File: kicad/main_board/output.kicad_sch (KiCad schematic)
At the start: 12 parts, among them J10 CH4, J4 DRV1, J5 DRV2, J6 CH_IN, J7 CH1, J8 CH2, J9 CH3

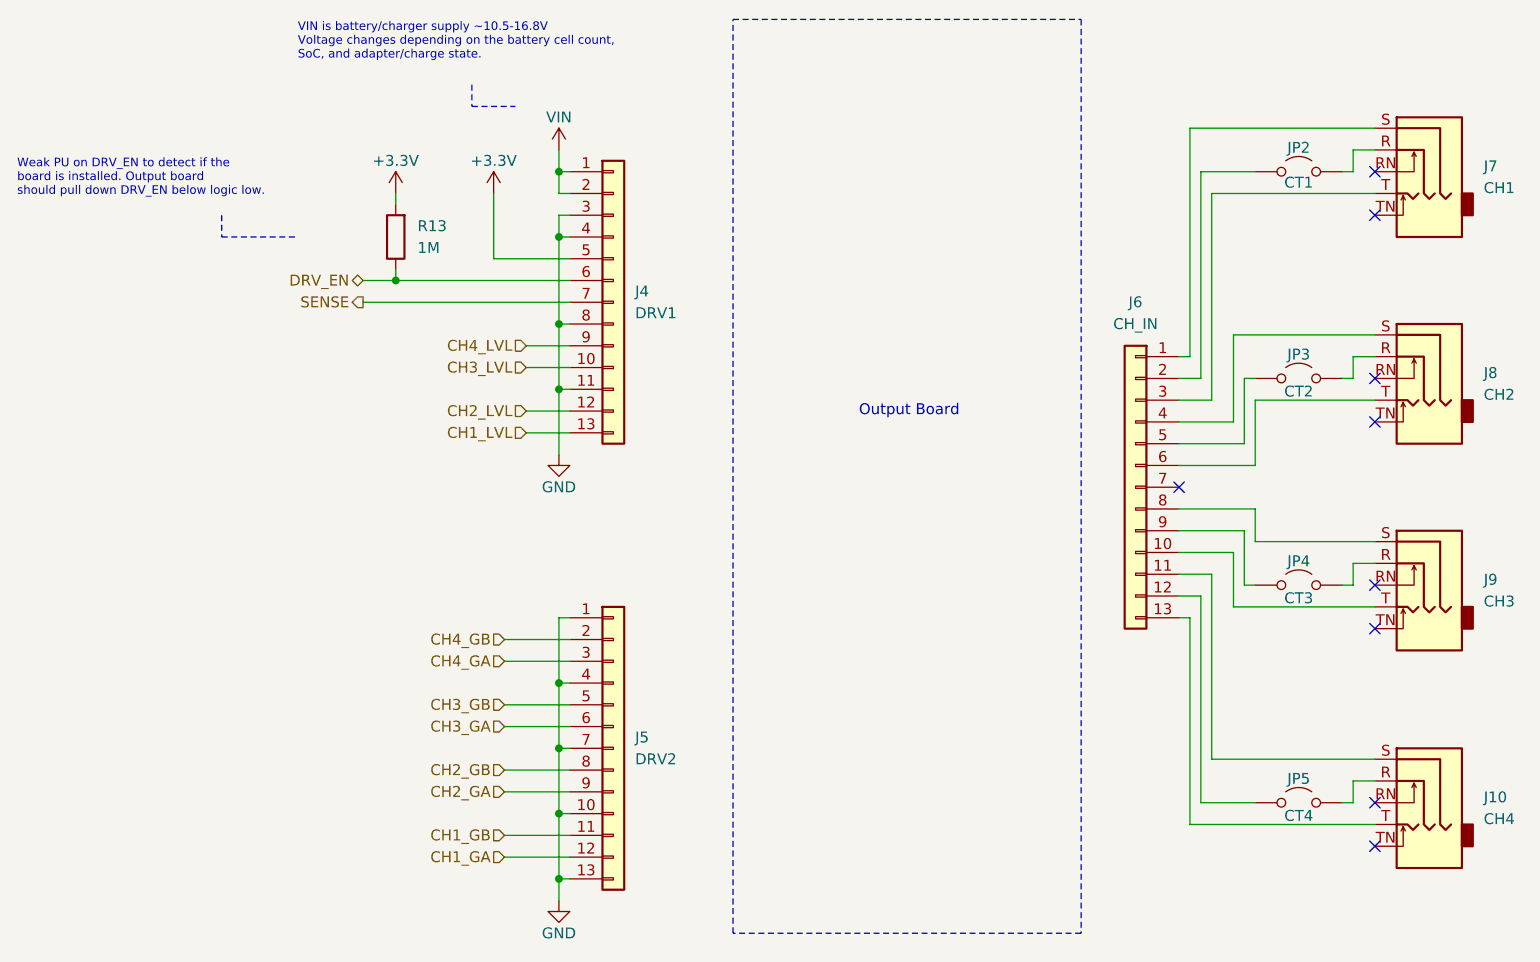
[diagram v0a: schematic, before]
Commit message: add input
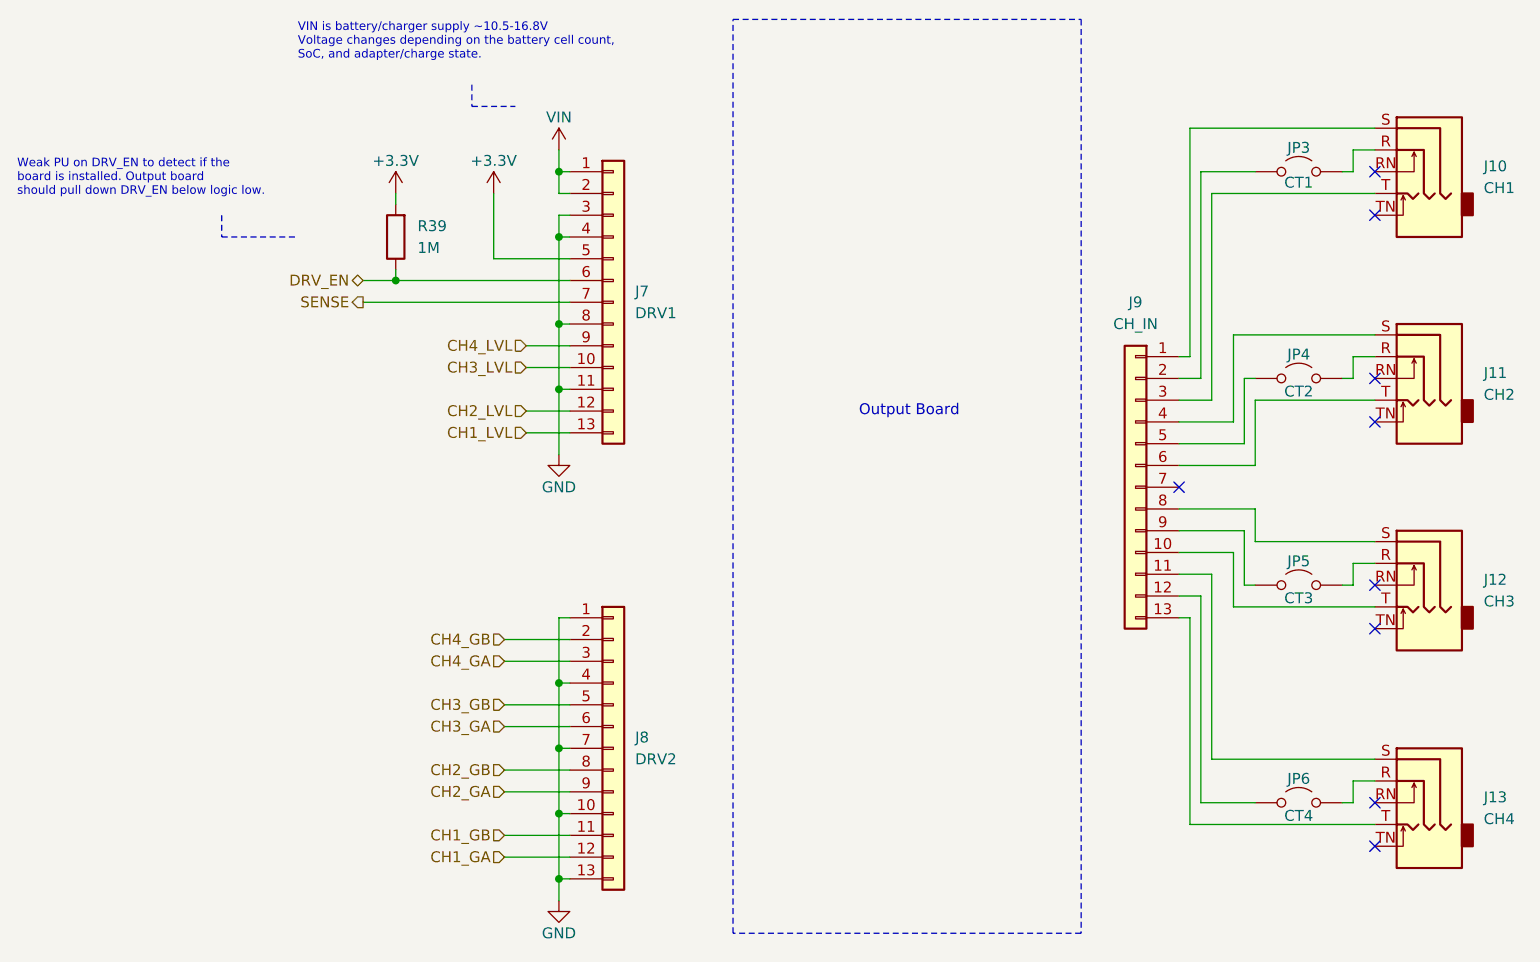
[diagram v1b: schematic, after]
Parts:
- renumbered J7 to J10, J8 to J11, J9 to J12, J10 to J13, J4 to J7, J5 to J8, J6 to J9, JP2 to JP3, JP3 to JP4, JP4 to JP5, JP5 to JP6, R13 to R39
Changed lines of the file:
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@@
 		(on_board yes)
 		(dnp no)
-		(property "Reference" "JP4"
+		(property "Reference" "JP5"
 			(at 198.12 101.346 0)
 			(effects
@@
 			(project "main_board"
 				(path "/8e1f1504-76c2-49e6-9261-3c1190503f8c/1327ee6b-7a00-44f7-81fe-b42319e4569a"
-					(reference "JP4")
+					(reference "JP5")
 					(unit 1)
 				)
@@
 		(dnp no)
 		(fields_autoplaced yes)
-		(property "Reference" "J4"
+		(property "Reference" "J7"
 			(at 120.65 69.8499 0)
 			(effects
@@
 			(project "main_board"
 				(path "/8e1f1504-76c2-49e6-9261-3c1190503f8c/1327ee6b-7a00-44f7-81fe-b42319e4569a"
-					(reference "J4")
+					(reference "J7")
 					(unit 1)
 				)
@@
 		(dnp no)
 		(fields_autoplaced yes)
-		(property "Reference" "J5"
+		(property "Reference" "J8"
 			(at 120.65 121.9199 0)
 			(effects
@@
 			(project "main_board"
 				(path "/8e1f1504-76c2-49e6-9261-3c1190503f8c/1327ee6b-7a00-44f7-81fe-b42319e4569a"
-					(reference "J5")
+					(reference "J8")
 					(unit 1)
 				)
@@
 		(on_board yes)
 		(dnp no)
-		(property "Reference" "#PWR041"
+		(property "Reference" "#PWR0105"
 			(at 111.76 147.32 0)
 			(effects
@@
 			(project "main_board"
 				(path "/8e1f1504-76c2-49e6-9261-3c1190503f8c/1327ee6b-7a00-44f7-81fe-b42319e4569a"
-					(reference "#PWR041")
+					(reference "#PWR0105")
 					(unit 1)
 				)
@@
 		(on_board yes)
 		(dnp no)
-		(property "Reference" "#PWR038"
+		(property "Reference" "#PWR0102"
 			(at 104.14 62.23 0)
 			(effects
@@
 			(project "main_board"
 				(path "/8e1f1504-76c2-49e6-9261-3c1190503f8c/1327ee6b-7a00-44f7-81fe-b42319e4569a"
-					(reference "#PWR038")
+					(reference "#PWR0102")
 					(unit 1)
 				)
@@
 		(on_board yes)
 		(dnp no)
-		(property "Reference" "JP5"
+		(property "Reference" "JP6"
 			(at 198.12 126.746 0)
 			(effects
@@
 			(project "main_board"
 				(path "/8e1f1504-76c2-49e6-9261-3c1190503f8c/1327ee6b-7a00-44f7-81fe-b42319e4569a"
-					(reference "JP5")
+					(reference "JP6")
 					(unit 1)
 				)
@@
 		(dnp no)
 		(fields_autoplaced yes)
-		(property "Reference" "J10"
+		(property "Reference" "J13"
 			(at 219.71 128.9049 0)
 			(effects
@@
 			(project "main_board"
 				(path "/8e1f1504-76c2-49e6-9261-3c1190503f8c/1327ee6b-7a00-44f7-81fe-b42319e4569a"
-					(reference "J10")
+					(reference "J13")
 					(unit 1)
 				)
@@
 		(dnp no)
 		(fields_autoplaced yes)
-		(property "Reference" "R13"
+		(property "Reference" "R39"
 			(at 95.25 62.2299 0)
 			(effects
@@
 			(project "main_board"
 				(path "/8e1f1504-76c2-49e6-9261-3c1190503f8c/1327ee6b-7a00-44f7-81fe-b42319e4569a"
-					(reference "R13")
+					(reference "R39")
 					(unit 1)
 				)
@@
 		(dnp no)
 		(fields_autoplaced yes)
-		(property "Reference" "J6"
+		(property "Reference" "J9"
 			(at 179.07 71.12 0)
 			(effects
@@
 			(project "main_board"
 				(path "/8e1f1504-76c2-49e6-9261-3c1190503f8c/1327ee6b-7a00-44f7-81fe-b42319e4569a"
-					(reference "J6")
+					(reference "J9")
 					(unit 1)
 				)
@@
 		(on_board yes)
 		(dnp no)
-		(property "Reference" "#PWR037"
+		(property "Reference" "#PWR0101"
 			(at 92.71 62.23 0)
 			(effects
@@
 			(project "main_board"
 				(path "/8e1f1504-76c2-49e6-9261-3c1190503f8c/1327ee6b-7a00-44f7-81fe-b42319e4569a"
-					(reference "#PWR037")
+					(reference "#PWR0101")
 					(unit 1)
 				)
@@
 		(on_board yes)
 		(dnp no)
-		(property "Reference" "JP2"
+		(property "Reference" "JP3"
 			(at 198.12 53.086 0)
 			(effects
@@
 			(project "main_board"
 				(path "/8e1f1504-76c2-49e6-9261-3c1190503f8c/1327ee6b-7a00-44f7-81fe-b42319e4569a"
-					(reference "JP2")
+					(reference "JP3")
 					(unit 1)
 				)
@@
 		(on_board yes)
 		(dnp no)
-		(property "Reference" "#PWR039"
+		(property "Reference" "#PWR0103"
 			(at 111.76 57.15 0)
 			(effects
@@
 			(project "main_board"
 				(path "/8e1f1504-76c2-49e6-9261-3c1190503f8c/1327ee6b-7a00-44f7-81fe-b42319e4569a"
-					(reference "#PWR039")
+					(reference "#PWR0103")
 					(unit 1)
 				)
@@
 		(dnp no)
 		(fields_autoplaced yes)
-		(property "Reference" "J7"
+		(property "Reference" "J10"
 			(at 219.71 55.2449 0)
 			(effects
@@
 			(project "main_board"
 				(path "/8e1f1504-76c2-49e6-9261-3c1190503f8c/1327ee6b-7a00-44f7-81fe-b42319e4569a"
-					(reference "J7")
+					(reference "J10")
 					(unit 1)
 				)
@@
 		(on_board yes)
 		(dnp no)
-		(property "Reference" "JP3"
+		(property "Reference" "JP4"
 			(at 198.12 77.216 0)
 			(effects
@@
 			(project "main_board"
 				(path "/8e1f1504-76c2-49e6-9261-3c1190503f8c/1327ee6b-7a00-44f7-81fe-b42319e4569a"
-					(reference "JP3")
+					(reference "JP4")
 					(unit 1)
 				)
@@
 		(dnp no)
 		(fields_autoplaced yes)
-		(property "Reference" "J8"
+		(property "Reference" "J11"
 			(at 219.71 79.3749 0)
 			(effects
@@
 			(project "main_board"
 				(path "/8e1f1504-76c2-49e6-9261-3c1190503f8c/1327ee6b-7a00-44f7-81fe-b42319e4569a"
-					(reference "J8")
+					(reference "J11")
 					(unit 1)
 				)
@@
 		(on_board yes)
 		(dnp no)
-		(property "Reference" "#PWR040"
+		(property "Reference" "#PWR0104"
 			(at 111.76 95.25 0)
 			(effects
@@
 			(project "main_board"
 				(path "/8e1f1504-76c2-49e6-9261-3c1190503f8c/1327ee6b-7a00-44f7-81fe-b42319e4569a"
-					(reference "#PWR040")
+					(reference "#PWR0104")
 					(unit 1)
 				)
@@
 		(dnp no)
 		(fields_autoplaced yes)
-		(property "Reference" "J9"
+		(property "Reference" "J12"
 			(at 219.71 103.5049 0)
 			(effects
@@
 			(project "main_board"
 				(path "/8e1f1504-76c2-49e6-9261-3c1190503f8c/1327ee6b-7a00-44f7-81fe-b42319e4569a"
-					(reference "J9")
+					(reference "J12")
 					(unit 1)
 				)

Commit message: add audio
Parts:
- renumbered J7 to J10, J8 to J11, J9 to J12, J10 to J13, J11 to J14, J12 to J15, J13 to J16, R39 to R64
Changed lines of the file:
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@@
 		(dnp no)
 		(fields_autoplaced yes)
-		(property "Reference" "J7"
+		(property "Reference" "J10"
 			(at 120.65 69.8499 0)
 			(effects
@@
 			(project "main_board"
 				(path "/8e1f1504-76c2-49e6-9261-3c1190503f8c/1327ee6b-7a00-44f7-81fe-b42319e4569a"
-					(reference "J7")
+					(reference "J10")
 					(unit 1)
 				)
@@
 		(dnp no)
 		(fields_autoplaced yes)
-		(property "Reference" "J8"
+		(property "Reference" "J11"
 			(at 120.65 121.9199 0)
 			(effects
@@
 			(project "main_board"
 				(path "/8e1f1504-76c2-49e6-9261-3c1190503f8c/1327ee6b-7a00-44f7-81fe-b42319e4569a"
-					(reference "J8")
+					(reference "J11")
 					(unit 1)
 				)
@@
 		(on_board yes)
 		(dnp no)
-		(property "Reference" "#PWR0105"
+		(property "Reference" "#PWR0147"
 			(at 111.76 147.32 0)
 			(effects
@@
 			(project "main_board"
 				(path "/8e1f1504-76c2-49e6-9261-3c1190503f8c/1327ee6b-7a00-44f7-81fe-b42319e4569a"
-					(reference "#PWR0105")
+					(reference "#PWR0147")
 					(unit 1)
 				)
@@
 		(on_board yes)
 		(dnp no)
-		(property "Reference" "#PWR0102"
+		(property "Reference" "#PWR0144"
 			(at 104.14 62.23 0)
 			(effects
@@
 			(project "main_board"
 				(path "/8e1f1504-76c2-49e6-9261-3c1190503f8c/1327ee6b-7a00-44f7-81fe-b42319e4569a"
-					(reference "#PWR0102")
+					(reference "#PWR0144")
 					(unit 1)
 				)
@@
 		(dnp no)
 		(fields_autoplaced yes)
-		(property "Reference" "J13"
+		(property "Reference" "J16"
 			(at 219.71 128.9049 0)
 			(effects
@@
 			)
 		)
-		(property "Datasheet" "~"
+		(property "Datasheet" "https://www.kycon.com/Pub_Eng_Draw/STX-3100-5N.pdf"
 			(at 212.09 127 0)
 			(effects
@@
 			(project "main_board"
 				(path "/8e1f1504-76c2-49e6-9261-3c1190503f8c/1327ee6b-7a00-44f7-81fe-b42319e4569a"
-					(reference "J13")
+					(reference "J16")
 					(unit 1)
 				)
@@
 		(dnp no)
 		(fields_autoplaced yes)
-		(property "Reference" "R39"
+		(property "Reference" "R64"
 			(at 95.25 62.2299 0)
 			(effects
@@
 			(project "main_board"
 				(path "/8e1f1504-76c2-49e6-9261-3c1190503f8c/1327ee6b-7a00-44f7-81fe-b42319e4569a"
-					(reference "R39")
+					(reference "R64")
 					(unit 1)
 				)
@@
 		(dnp no)
 		(fields_autoplaced yes)
-		(property "Reference" "J9"
+		(property "Reference" "J12"
 			(at 179.07 71.12 0)
 			(effects
@@
 			(project "main_board"
 				(path "/8e1f1504-76c2-49e6-9261-3c1190503f8c/1327ee6b-7a00-44f7-81fe-b42319e4569a"
-					(reference "J9")
+					(reference "J12")
 					(unit 1)
 				)
@@
 		(on_board yes)
 		(dnp no)
-		(property "Reference" "#PWR0101"
+		(property "Reference" "#PWR0143"
 			(at 92.71 62.23 0)
 			(effects
@@
 			(project "main_board"
 				(path "/8e1f1504-76c2-49e6-9261-3c1190503f8c/1327ee6b-7a00-44f7-81fe-b42319e4569a"
-					(reference "#PWR0101")
+					(reference "#PWR0143")
 					(unit 1)
 				)
@@
 		(on_board yes)
 		(dnp no)
-		(property "Reference" "#PWR0103"
+		(property "Reference" "#PWR0145"
 			(at 111.76 57.15 0)
 			(effects
@@
 			(project "main_board"
 				(path "/8e1f1504-76c2-49e6-9261-3c1190503f8c/1327ee6b-7a00-44f7-81fe-b42319e4569a"
-					(reference "#PWR0103")
+					(reference "#PWR0145")
 					(unit 1)
 				)
@@
 		(dnp no)
 		(fields_autoplaced yes)
-		(property "Reference" "J10"
+		(property "Reference" "J13"
 			(at 219.71 55.2449 0)
 			(effects
@@
 			)
 		)
-		(property "Datasheet" "~"
+		(property "Datasheet" "https://www.kycon.com/Pub_Eng_Draw/STX-3100-5N.pdf"
 			(at 212.09 53.34 0)
 			(effects
@@
 			(project "main_board"
 				(path "/8e1f1504-76c2-49e6-9261-3c1190503f8c/1327ee6b-7a00-44f7-81fe-b42319e4569a"
-					(reference "J10")
+					(reference "J13")
 					(unit 1)
 				)
@@
 		(dnp no)
 		(fields_autoplaced yes)
-		(property "Reference" "J11"
+		(property "Reference" "J14"
 			(at 219.71 79.3749 0)
 			(effects
@@
 			)
 		)
-		(property "Datasheet" "~"
+		(property "Datasheet" "https://www.kycon.com/Pub_Eng_Draw/STX-3100-5N.pdf"
 			(at 212.09 77.47 0)
 			(effects
@@
 			(project "main_board"
 				(path "/8e1f1504-76c2-49e6-9261-3c1190503f8c/1327ee6b-7a00-44f7-81fe-b42319e4569a"
-					(reference "J11")
+					(reference "J14")
 					(unit 1)
 				)
@@
 		(on_board yes)
 		(dnp no)
-		(property "Reference" "#PWR0104"
+		(property "Reference" "#PWR0146"
 			(at 111.76 95.25 0)
 			(effects
@@
 			(project "main_board"
 				(path "/8e1f1504-76c2-49e6-9261-3c1190503f8c/1327ee6b-7a00-44f7-81fe-b42319e4569a"
-					(reference "#PWR0104")
+					(reference "#PWR0146")
 					(unit 1)
 				)
@@
 		(dnp no)
 		(fields_autoplaced yes)
-		(property "Reference" "J12"
+		(property "Reference" "J15"
 			(at 219.71 103.5049 0)
 			(effects
@@
 			)
 		)
-		(property "Datasheet" "~"
+		(property "Datasheet" "https://www.kycon.com/Pub_Eng_Draw/STX-3100-5N.pdf"
 			(at 212.09 101.6 0)
 			(effects
@@
 			(project "main_board"
 				(path "/8e1f1504-76c2-49e6-9261-3c1190503f8c/1327ee6b-7a00-44f7-81fe-b42319e4569a"
-					(reference "J12")
+					(reference "J15")
 					(unit 1)
 				)

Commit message: add charger
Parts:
- renumbered J10 to J12, J11 to J13, J12 to J14, J13 to J15, J14 to J16, J15 to J17, J16 to J18, JP3 to JP4, JP4 to JP5, JP5 to JP6, JP6 to JP7, R64 to R83
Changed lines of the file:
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@@
 		(on_board yes)
 		(dnp no)
-		(property "Reference" "JP5"
+		(property "Reference" "JP6"
 			(at 198.12 101.346 0)
 			(effects
@@
 			(project "main_board"
 				(path "/8e1f1504-76c2-49e6-9261-3c1190503f8c/1327ee6b-7a00-44f7-81fe-b42319e4569a"
-					(reference "JP5")
+					(reference "JP6")
 					(unit 1)
 				)
@@
 		(dnp no)
 		(fields_autoplaced yes)
-		(property "Reference" "J10"
+		(property "Reference" "J12"
 			(at 120.65 69.8499 0)
 			(effects
@@
 			(project "main_board"
 				(path "/8e1f1504-76c2-49e6-9261-3c1190503f8c/1327ee6b-7a00-44f7-81fe-b42319e4569a"
-					(reference "J10")
+					(reference "J12")
 					(unit 1)
 				)
@@
 		(dnp no)
 		(fields_autoplaced yes)
-		(property "Reference" "J11"
+		(property "Reference" "J13"
 			(at 120.65 121.9199 0)
 			(effects
@@
 			(project "main_board"
 				(path "/8e1f1504-76c2-49e6-9261-3c1190503f8c/1327ee6b-7a00-44f7-81fe-b42319e4569a"
-					(reference "J11")
+					(reference "J13")
 					(unit 1)
 				)
@@
 		(on_board yes)
 		(dnp no)
-		(property "Reference" "#PWR0147"
+		(property "Reference" "#PWR0179"
 			(at 111.76 147.32 0)
 			(effects
@@
 			(project "main_board"
 				(path "/8e1f1504-76c2-49e6-9261-3c1190503f8c/1327ee6b-7a00-44f7-81fe-b42319e4569a"
-					(reference "#PWR0147")
+					(reference "#PWR0179")
 					(unit 1)
 				)
@@
 		(on_board yes)
 		(dnp no)
-		(property "Reference" "#PWR0144"
+		(property "Reference" "#PWR0176"
 			(at 104.14 62.23 0)
 			(effects
@@
 			(project "main_board"
 				(path "/8e1f1504-76c2-49e6-9261-3c1190503f8c/1327ee6b-7a00-44f7-81fe-b42319e4569a"
-					(reference "#PWR0144")
+					(reference "#PWR0176")
 					(unit 1)
 				)
@@
 		(on_board yes)
 		(dnp no)
-		(property "Reference" "JP6"
+		(property "Reference" "JP7"
 			(at 198.12 126.746 0)
 			(effects
@@
 			(project "main_board"
 				(path "/8e1f1504-76c2-49e6-9261-3c1190503f8c/1327ee6b-7a00-44f7-81fe-b42319e4569a"
-					(reference "JP6")
+					(reference "JP7")
 					(unit 1)
 				)
@@
 		(dnp no)
 		(fields_autoplaced yes)
-		(property "Reference" "J16"
+		(property "Reference" "J18"
 			(at 219.71 128.9049 0)
 			(effects
@@
 			(project "main_board"
 				(path "/8e1f1504-76c2-49e6-9261-3c1190503f8c/1327ee6b-7a00-44f7-81fe-b42319e4569a"
-					(reference "J16")
+					(reference "J18")
 					(unit 1)
 				)
@@
 		(dnp no)
 		(fields_autoplaced yes)
-		(property "Reference" "R64"
+		(property "Reference" "R83"
 			(at 95.25 62.2299 0)
 			(effects
@@
 			(project "main_board"
 				(path "/8e1f1504-76c2-49e6-9261-3c1190503f8c/1327ee6b-7a00-44f7-81fe-b42319e4569a"
-					(reference "R64")
+					(reference "R83")
 					(unit 1)
 				)
@@
 		(dnp no)
 		(fields_autoplaced yes)
-		(property "Reference" "J12"
+		(property "Reference" "J14"
 			(at 179.07 71.12 0)
 			(effects
@@
 			(project "main_board"
 				(path "/8e1f1504-76c2-49e6-9261-3c1190503f8c/1327ee6b-7a00-44f7-81fe-b42319e4569a"
-					(reference "J12")
+					(reference "J14")
 					(unit 1)
 				)
@@
 		(on_board yes)
 		(dnp no)
-		(property "Reference" "#PWR0143"
+		(property "Reference" "#PWR0175"
 			(at 92.71 62.23 0)
 			(effects
@@
 			(project "main_board"
 				(path "/8e1f1504-76c2-49e6-9261-3c1190503f8c/1327ee6b-7a00-44f7-81fe-b42319e4569a"
-					(reference "#PWR0143")
+					(reference "#PWR0175")
 					(unit 1)
 				)
@@
 		(on_board yes)
 		(dnp no)
-		(property "Reference" "JP3"
+		(property "Reference" "JP4"
 			(at 198.12 53.086 0)
 			(effects
@@
 			(project "main_board"
 				(path "/8e1f1504-76c2-49e6-9261-3c1190503f8c/1327ee6b-7a00-44f7-81fe-b42319e4569a"
-					(reference "JP3")
+					(reference "JP4")
 					(unit 1)
 				)
@@
 		(on_board yes)
 		(dnp no)
-		(property "Reference" "#PWR0145"
+		(property "Reference" "#PWR0177"
 			(at 111.76 57.15 0)
 			(effects
@@
 			(project "main_board"
 				(path "/8e1f1504-76c2-49e6-9261-3c1190503f8c/1327ee6b-7a00-44f7-81fe-b42319e4569a"
-					(reference "#PWR0145")
+					(reference "#PWR0177")
 					(unit 1)
 				)
@@
 		(dnp no)
 		(fields_autoplaced yes)
-		(property "Reference" "J13"
+		(property "Reference" "J15"
 			(at 219.71 55.2449 0)
 			(effects
@@
 			(project "main_board"
 				(path "/8e1f1504-76c2-49e6-9261-3c1190503f8c/1327ee6b-7a00-44f7-81fe-b42319e4569a"
-					(reference "J13")
+					(reference "J15")
 					(unit 1)
 				)
@@
 		(on_board yes)
 		(dnp no)
-		(property "Reference" "JP4"
+		(property "Reference" "JP5"
 			(at 198.12 77.216 0)
 			(effects
@@
 			(project "main_board"
 				(path "/8e1f1504-76c2-49e6-9261-3c1190503f8c/1327ee6b-7a00-44f7-81fe-b42319e4569a"
-					(reference "JP4")
+					(reference "JP5")
 					(unit 1)
 				)
@@
 		(dnp no)
 		(fields_autoplaced yes)
-		(property "Reference" "J14"
+		(property "Reference" "J16"
 			(at 219.71 79.3749 0)
 			(effects
@@
 			(project "main_board"
 				(path "/8e1f1504-76c2-49e6-9261-3c1190503f8c/1327ee6b-7a00-44f7-81fe-b42319e4569a"
-					(reference "J14")
+					(reference "J16")
 					(unit 1)
 				)
@@
 		(on_board yes)
 		(dnp no)
-		(property "Reference" "#PWR0146"
+		(property "Reference" "#PWR0178"
 			(at 111.76 95.25 0)
 			(effects
@@
 			(project "main_board"
 				(path "/8e1f1504-76c2-49e6-9261-3c1190503f8c/1327ee6b-7a00-44f7-81fe-b42319e4569a"
-					(reference "#PWR0146")
+					(reference "#PWR0178")
 					(unit 1)
 				)
@@
 		(dnp no)
 		(fields_autoplaced yes)
-		(property "Reference" "J15"
+		(property "Reference" "J17"
 			(at 219.71 103.5049 0)
 			(effects
@@
 			(project "main_board"
 				(path "/8e1f1504-76c2-49e6-9261-3c1190503f8c/1327ee6b-7a00-44f7-81fe-b42319e4569a"
-					(reference "J15")
+					(reference "J17")
 					(unit 1)
 				)
